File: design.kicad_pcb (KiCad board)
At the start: 2 copper layers, 35.5 x 15 mm, 21 parts, among them J1 USB_C_Receptacle, J2 Conn_01x05, Q1 2N7002K, Q2 2N7002K, Q3 2N7002K, U1 ATtiny814-SS

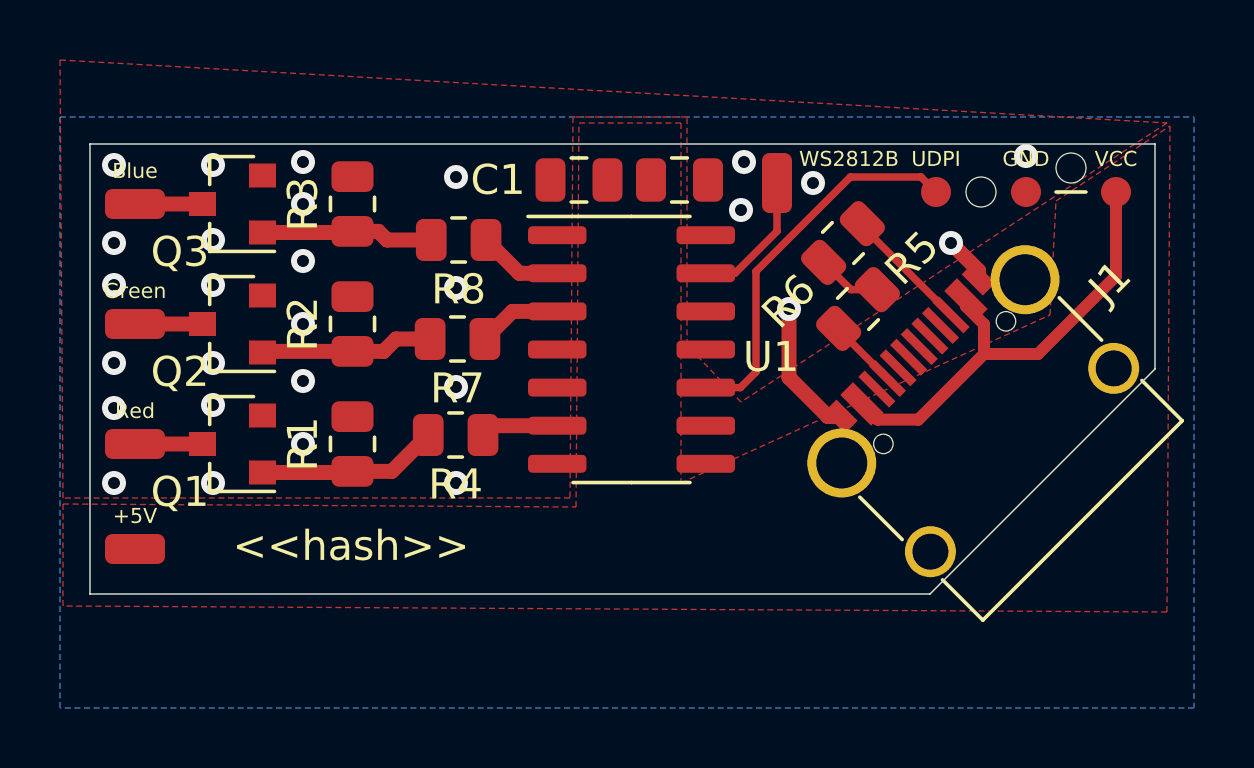
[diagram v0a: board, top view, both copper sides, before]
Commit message: PCB: refined GND plane
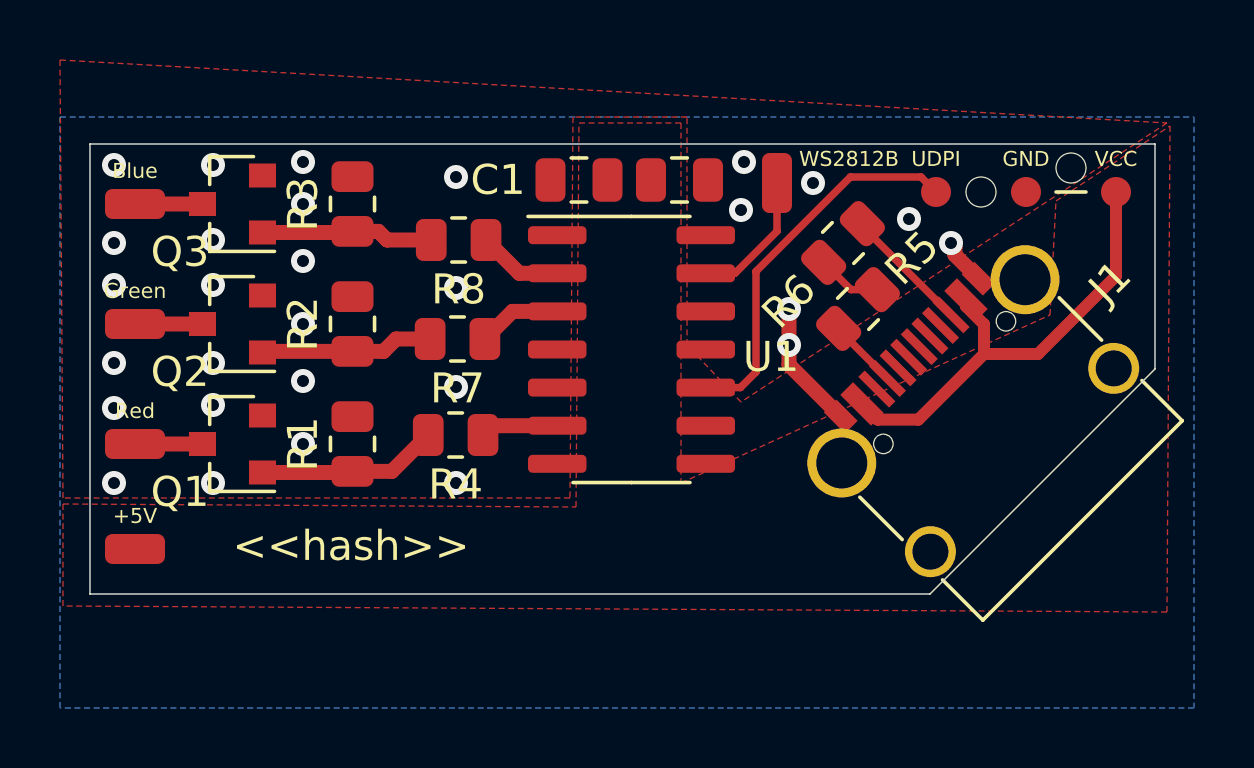
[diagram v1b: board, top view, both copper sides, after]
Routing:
- net GND: track 8.28 -> 8.04 mm, vias 28 -> 29
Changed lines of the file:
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@@
     (thickness 1.6)
     (drawings 12)
-    (tracks 81)
+    (tracks 83)
     (zones 0)
     (modules 21)
@@
   )
   (setup
-    (last_trace_width 0.4)
+    (last_trace_width 0.5)
     (user_trace_width 0.4)
     (user_trace_width 0.5)
@@
   (segment (start 162.745235 84.854765) (end 161.864295 84.854765) (width 0.25) (layer F.Cu) (net 15))
   (via (at 159.8 85.5) (size 0.8) (drill 0.4) (layers F.Cu B.Cu) (net 15))
-  (segment (start 166.119854 84.219854) (end 165.2 83.3) (width 0.5) (layer F.Cu) (net 15))
-  (segment (start 166.119854 84.488475) (end 166.119854 84.219854) (width 0.5) (layer F.Cu) (net 15))
-  (segment (start 161.099396 89.084669) (end 159.8 87.785273) (width 0.5) (layer F.Cu) (net 15))
-  (segment (start 159.8 87.785273) (end 159.8 85.5) (width 0.5) (layer F.Cu) (net 15))
-  (segment (start 161.52366 89.084669) (end 161.099396 89.084669) (width 0.5) (layer F.Cu) (net 15))
   (via (at 143.6 82) (size 0.8) (drill 0.4) (layers F.Cu B.Cu) (net 15))
   (via (at 143.6 80.6) (size 0.8) (drill 0.4) (layers F.Cu B.Cu) (net 15))
@@
   (via (at 140.6 91.3) (size 0.8) (drill 0.4) (layers F.Cu B.Cu) (net 15))
   (via (at 137.3 91.3) (size 0.8) (drill 0.4) (layers F.Cu B.Cu) (net 15))
-  (via (at 167.7 80.4) (size 0.8) (drill 0.4) (layers F.Cu B.Cu) (net 15))
+  (segment (start 159.8 87.361009) (end 159.8 86.7) (width 0.5) (layer F.Cu) (net 15))
+  (segment (start 161.52366 89.084669) (end 159.8 87.361009) (width 0.5) (layer F.Cu) (net 15))
+  (segment (start 166.119854 84.488475) (end 165.331379 83.7) (width 0.5) (layer F.Cu) (net 15))
+  (segment (start 165.331379 83.431379) (end 165.2 83.3) (width 0.5) (layer F.Cu) (net 15))
+  (segment (start 165.331379 83.7) (end 165.331379 83.431379) (width 0.5) (layer F.Cu) (net 15))
+  (segment (start 159.8 86.7) (end 159.8 85.5) (width 0.5) (layer F.Cu) (net 15))
+  (via (at 159.8 86.7) (size 0.8) (drill 0.4) (layers F.Cu B.Cu) (net 15))
+  (via (at 163.8 82.5) (size 0.8) (drill 0.4) (layers F.Cu B.Cu) (net 15))
   (segment (start 149.91 89.39) (end 149.6 89.7) (width 0.5) (layer F.Cu) (net 16))
   (segment (start 152.075 89.39) (end 149.91 89.39) (width 0.5) (layer F.Cu) (net 16))

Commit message: PCB: added GND Vias
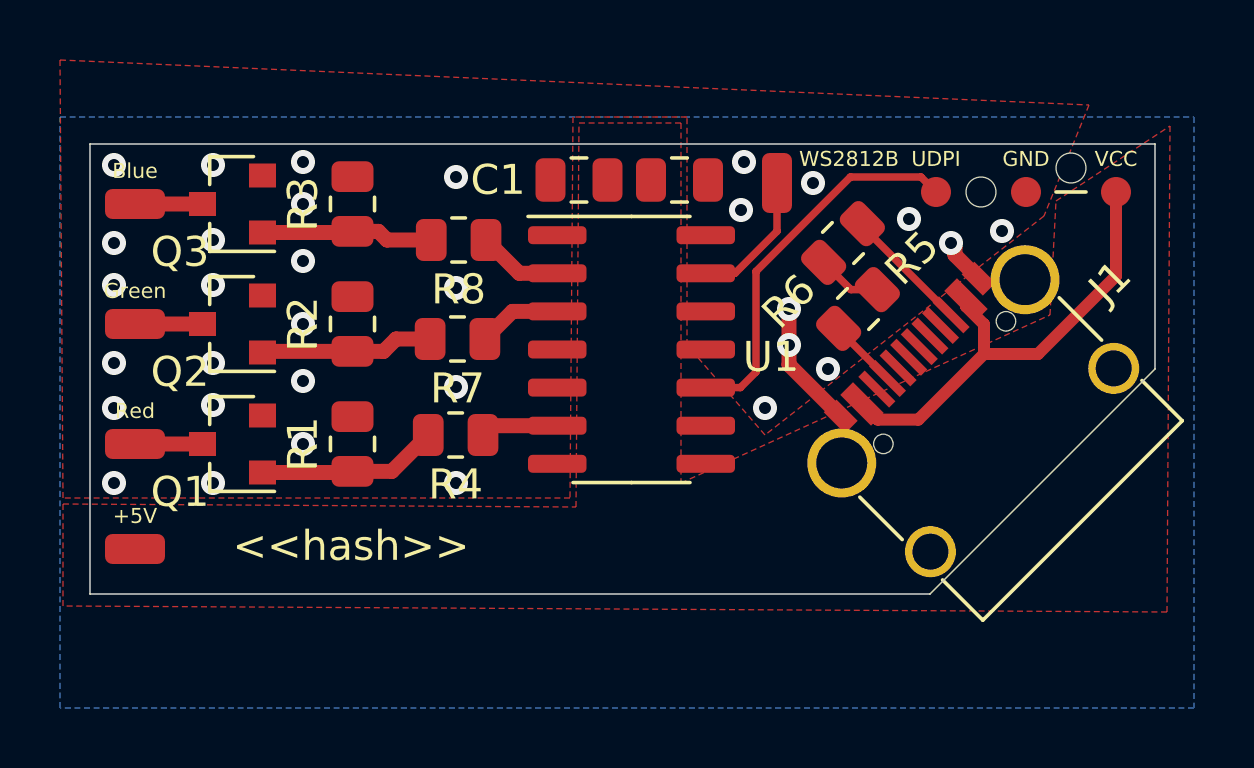
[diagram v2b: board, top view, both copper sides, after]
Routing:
- net GND: vias 29 -> 32
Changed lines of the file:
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@@
     (thickness 1.6)
     (drawings 12)
-    (tracks 83)
+    (tracks 86)
     (zones 0)
     (modules 21)
@@
   (gr_line (start 172 80) (end 172 87.5) (layer Edge.Cuts) (width 0.05))
   (gr_line (start 136.5 80) (end 172 80) (layer Edge.Cuts) (width 0.05))
+  (via (at 166.9 82.9) (size 0.8) (drill 0.4) (layers F.Cu B.Cu) (net 15))
   (via (at 160.6 81.3) (size 0.8) (drill 0.4) (layers F.Cu B.Cu) (net 15))
   (via (at 158.3 80.6) (size 0.8) (drill 0.4) (layers F.Cu B.Cu) (net 15))
@@
   (via (at 159.8 86.7) (size 0.8) (drill 0.4) (layers F.Cu B.Cu) (net 15))
   (via (at 163.8 82.5) (size 0.8) (drill 0.4) (layers F.Cu B.Cu) (net 15))
+  (via (at 159 88.8) (size 0.8) (drill 0.4) (layers F.Cu B.Cu) (net 15))
+  (via (at 161.1 87.5) (size 0.8) (drill 0.4) (layers F.Cu B.Cu) (net 15))
   (segment (start 149.91 89.39) (end 149.6 89.7) (width 0.5) (layer F.Cu) (net 16))
   (segment (start 152.075 89.39) (end 149.91 89.39) (width 0.5) (layer F.Cu) (net 16))
@@
     (polygon
       (pts
-        (xy 172.4 79.3) (xy 158.2 88.6) (xy 156.4 86.7) (xy 156.4 79.1) (xy 152.6 79.1)
-        (xy 152.5 91.8) (xy 135.6 91.8) (xy 135.5 77.2)
+        (xy 169.8 78.7) (xy 168.3 82.4) (xy 159 89.7) (xy 156.4 86.7) (xy 156.4 79.1)
+        (xy 152.6 79.1) (xy 152.5 91.8) (xy 135.6 91.8) (xy 135.5 77.2)
       )
     )

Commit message: PCB: changes due to DRC
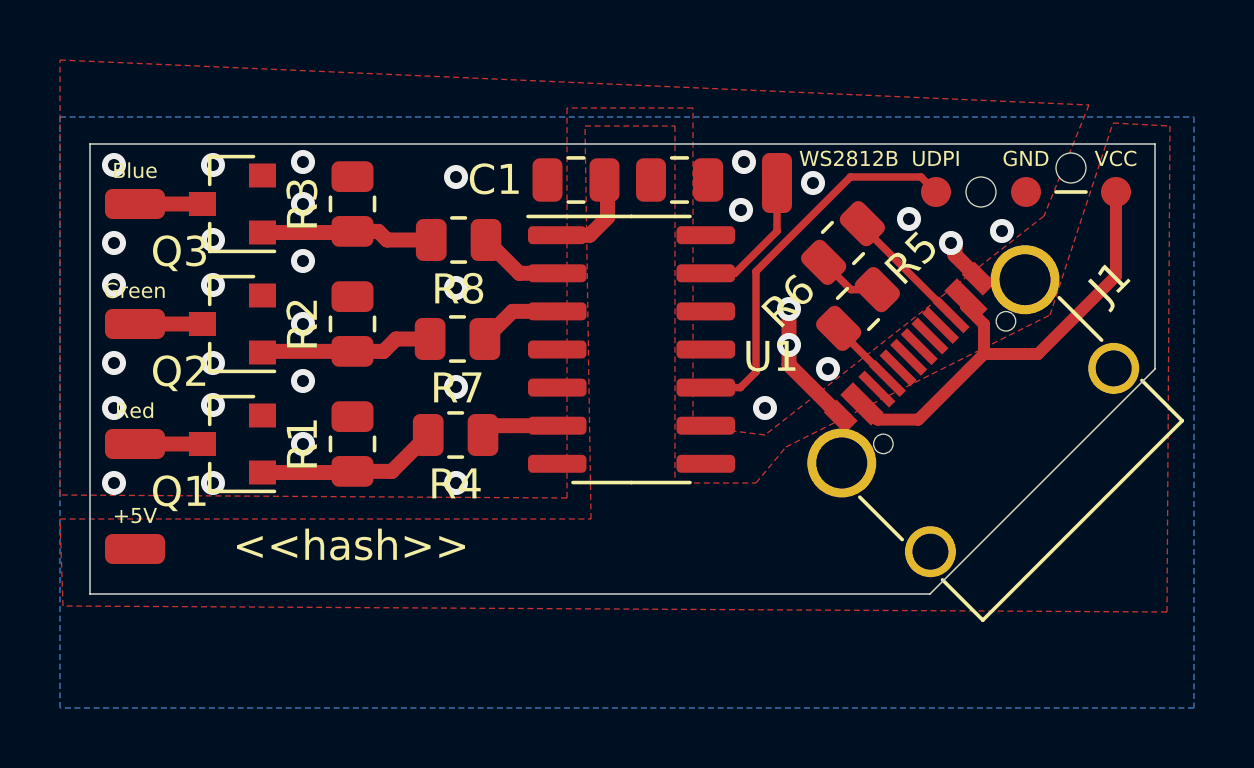
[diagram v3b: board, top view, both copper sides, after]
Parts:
- moved C1 0.10 mm to (152.7, 81.2)
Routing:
- net VCC: track 15.5 -> 18.7 mm
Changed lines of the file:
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@@
     (thickness 1.6)
     (drawings 12)
-    (tracks 86)
+    (tracks 89)
     (zones 0)
     (modules 21)
@@
   )
   (module Capacitor_SMD:C_0805_2012Metric (layer F.Cu)
-    (at 152.8 81.2 180)
+    (at 152.7 81.2 180)
     (descr "Capacitor SMD 0805 (2012 Metric), square (rectangular) end terminal, IPC_7351 nominal, (Body size source: IPC-SM-782 page 76, https://www.pcb-3d.com/wordpress/wp-content/uploads/ipc-sm-782a_amendment_1_and_2.pdf, https://docs.google.com/spreadsheets/d/1BsfQQcO9C6DZCsRaXUlFlo91Tg2WpOkGARC1WS5S8t0/edit?usp=sharing), generated with kicad-footprint-generator")
     (tags capacitor)
@@
   (segment (start 170.7 84.4) (end 168.1 87) (width 0.4) (layer F.Cu) (net 22))
   (segment (start 170.7 81.6) (end 170.7 84.4) (width 0.4) (layer F.Cu) (net 22))
+  (segment (start 153.75 81.2) (end 153.75 82.45) (width 0.5) (layer F.Cu) (net 22))
+  (segment (start 153.16 83.04) (end 152.075 83.04) (width 0.5) (layer F.Cu) (net 22))
+  (segment (start 153.75 82.45) (end 153.16 83.04) (width 0.5) (layer F.Cu) (net 22))
   (segment (start 157.025 88.12) (end 158.18 88.12) (width 0.25) (layer F.Cu) (net 25))
   (segment (start 158.7 87.6) (end 158.7 84.24641) (width 0.25) (layer F.Cu) (net 25))
@@
     (polygon
       (pts
-        (xy 169.8 78.7) (xy 168.3 82.4) (xy 159 89.7) (xy 156.4 86.7) (xy 156.4 79.1)
-        (xy 152.6 79.1) (xy 152.5 91.8) (xy 135.6 91.8) (xy 135.5 77.2)
+        (xy 169.8 78.7) (xy 168.3 82.4) (xy 159 89.7) (xy 156.6 89.4) (xy 156.6 78.8)
+        (xy 152.4 78.8) (xy 152.4 91.8) (xy 135.5 91.7) (xy 135.5 77.2)
       )
     )
@@
     (polygon
       (pts
-        (xy 168.5 85.7) (xy 168.7 81.9) (xy 172.5 79.4) (xy 172.4 95.6) (xy 135.6 95.4)
-        (xy 135.6 92) (xy 152.7 92.1) (xy 152.8 79.3) (xy 156.2 79.3) (xy 156.2 91.3)
+        (xy 158.7 91.3) (xy 159.7 90.1) (xy 168.5 85.7) (xy 170.6 79.3) (xy 172.5 79.4)
+        (xy 172.4 95.6) (xy 135.6 95.4) (xy 135.5 92.5) (xy 153.2 92.5) (xy 153 79.4)
+        (xy 156 79.4) (xy 156 91.3)
       )
     )

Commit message: PCB: change Fill on power path to solid
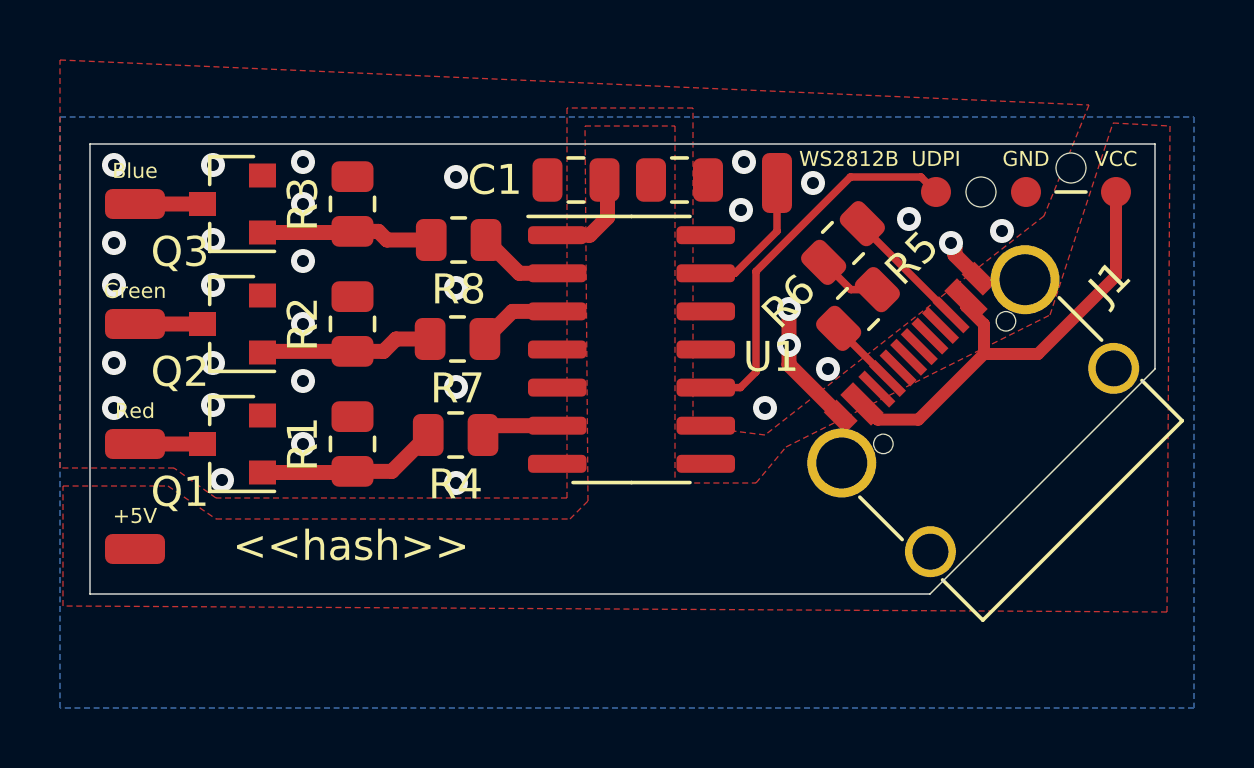
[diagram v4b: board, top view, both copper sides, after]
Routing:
- net GND: vias 32 -> 31
